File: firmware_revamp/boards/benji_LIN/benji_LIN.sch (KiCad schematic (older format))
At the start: 48 parts, among them J1 CONN_02X03, U1 MCP2561-E_SN, U101 TPS560430YF, U2 ATMEGA16M1, U3 TLIN1021DRQ1, Y1 Crystal_SMD

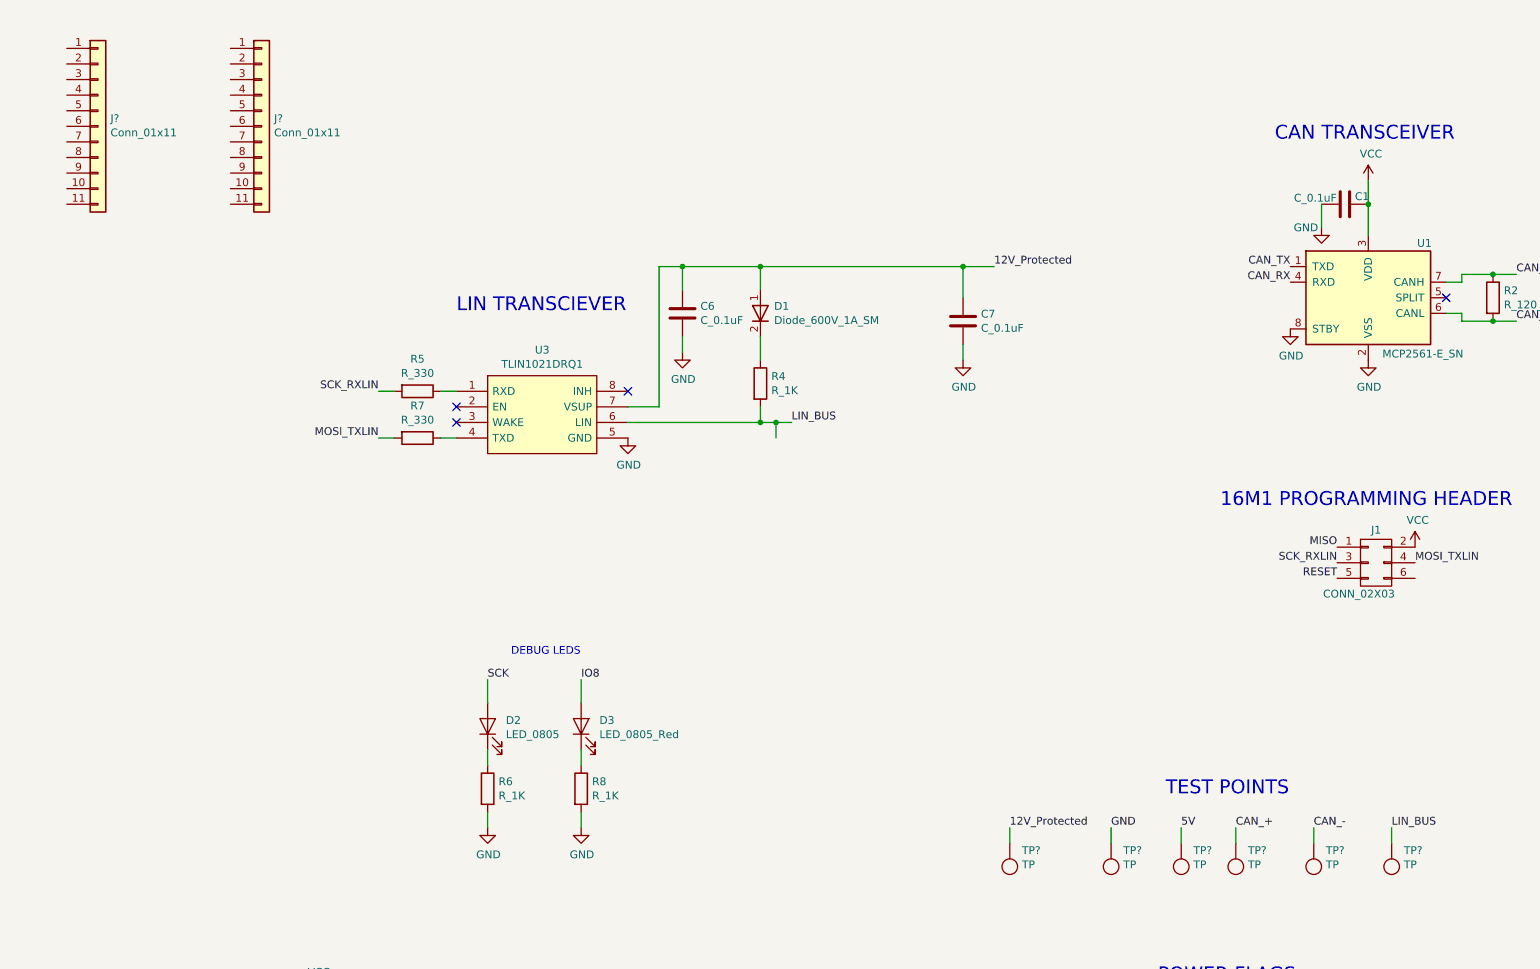
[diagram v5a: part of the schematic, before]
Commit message: Fixed name and title
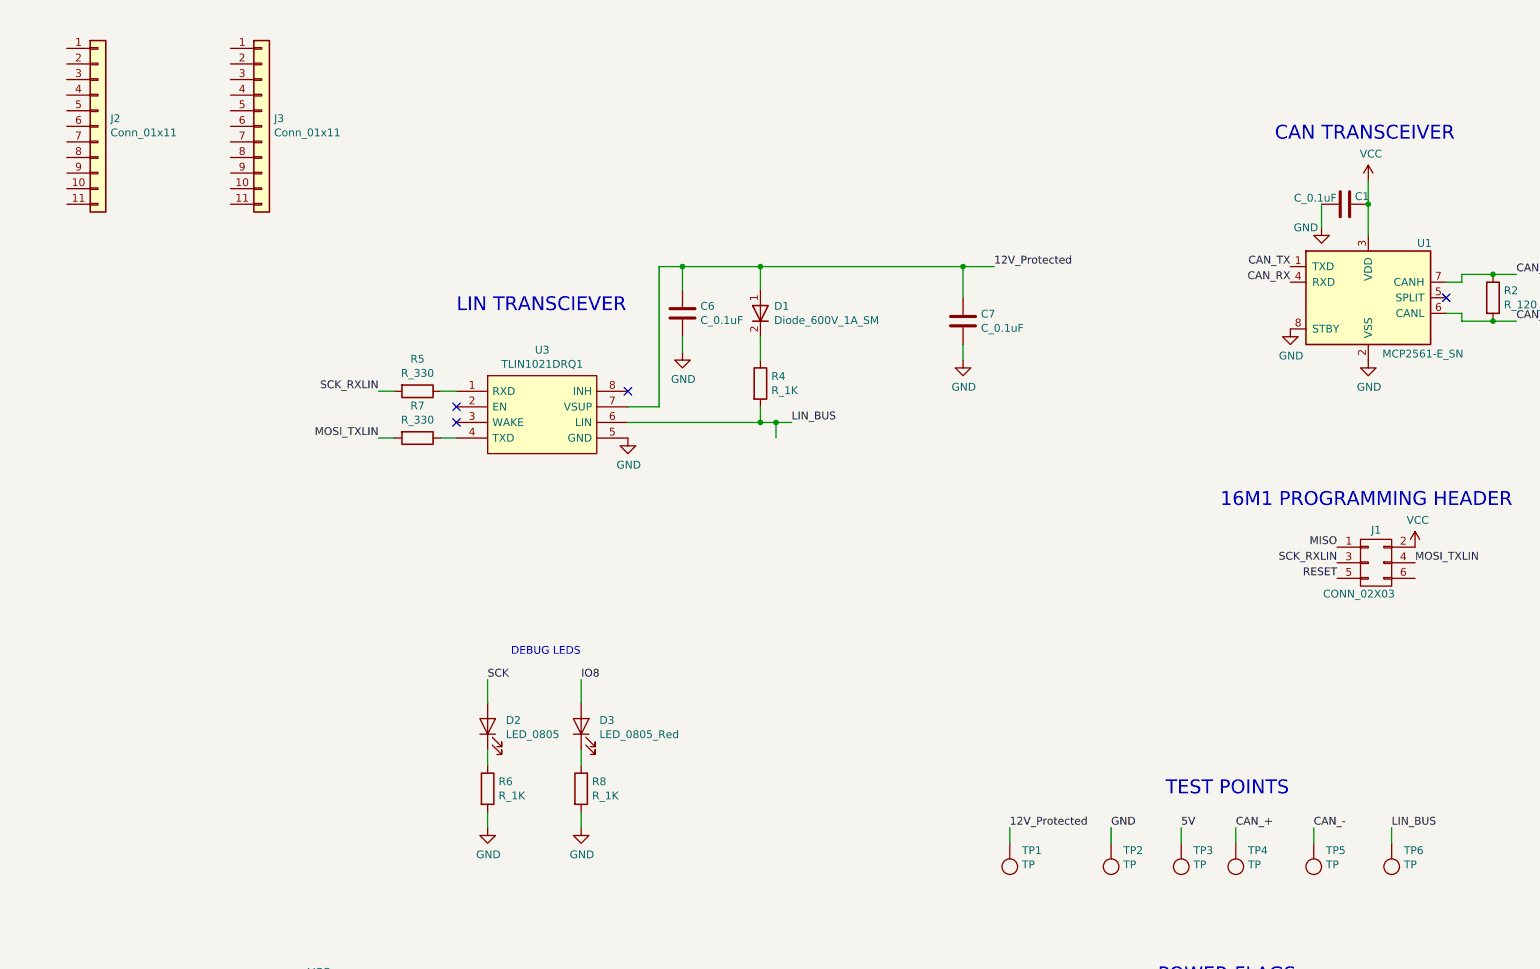
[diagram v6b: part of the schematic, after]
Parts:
- gave numbers to parts that had none: 8
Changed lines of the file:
@@
 encoding utf-8
 Sheet 1 1
-Title "OEM Project Template"
+Title "OEM LIN Hackerboard"
 Date "2019-08-22"
 Rev "1"
 Comp "Olin Electric Motorsports"
-Comment1 "Wesley Soo-Hoo"
+Comment1 "Benji Pugh"
 Comment2 ""
 Comment3 ""
@@
 	7850 3700 7950 3700
 $Comp
-L formula:Conn_01x11 J?
+L formula:Conn_01x11 J2
 U 1 1 603F6805
 P 5650 1750
-F 0 "J?" H 5730 1850 50  0000 L CNN
+F 0 "J2" H 5730 1850 50  0000 L CNN
 F 1 "Conn_01x11" H 5730 1759 50  0000 L CNN
 F 2 "footprints:PinHeader_1x11_P2.54mm_Vertical" H 5550 2450 50  0001 C CNN
@@
 $EndComp
 $Comp
-L formula:Conn_01x11 J?
+L formula:Conn_01x11 J3
 U 1 1 6040C0B1
 P 6700 1750
-F 0 "J?" H 6780 1850 50  0000 L CNN
+F 0 "J3" H 6780 1850 50  0000 L CNN
 F 1 "Conn_01x11" H 6780 1759 50  0000 L CNN
 F 2 "footprints:PinHeader_1x11_P2.54mm_Vertical" H 6600 2450 50  0001 C CNN
@@
 $EndComp
 $Comp
-L formula:TP TP?
+L formula:TP TP2
 U 1 1 6043188E
 P 12150 6500
-F 0 "TP?" H 12072 6346 50  0000 R CNN
+F 0 "TP2" H 12072 6346 50  0000 R CNN
 F 1 "TP" H 12072 6437 50  0000 R CNN
 F 2 "footprints:tp_1.6mm" H 12050 6400 50  0001 C CNN
@@
 $EndComp
 $Comp
-L formula:TP TP?
+L formula:TP TP3
 U 1 1 60452016
 P 12600 6500
-F 0 "TP?" H 12522 6346 50  0000 R CNN
+F 0 "TP3" H 12522 6346 50  0000 R CNN
 F 1 "TP" H 12522 6437 50  0000 R CNN
 F 2 "footprints:tp_1.6mm" H 12500 6400 50  0001 C CNN
@@
 $EndComp
 $Comp
-L formula:TP TP?
+L formula:TP TP4
 U 1 1 60452657
 P 12950 6500
-F 0 "TP?" H 12872 6346 50  0000 R CNN
+F 0 "TP4" H 12872 6346 50  0000 R CNN
 F 1 "TP" H 12872 6437 50  0000 R CNN
 F 2 "footprints:tp_1.6mm" H 12850 6400 50  0001 C CNN
@@
 $EndComp
 $Comp
-L formula:TP TP?
+L formula:TP TP5
 U 1 1 60452C4A
 P 13450 6500
-F 0 "TP?" H 13372 6346 50  0000 R CNN
+F 0 "TP5" H 13372 6346 50  0000 R CNN
 F 1 "TP" H 13372 6437 50  0000 R CNN
 F 2 "footprints:tp_1.6mm" H 13350 6400 50  0001 C CNN
@@
 $EndComp
 $Comp
-L formula:TP TP?
+L formula:TP TP6
 U 1 1 604534CE
 P 13950 6500
-F 0 "TP?" H 13872 6346 50  0000 R CNN
+F 0 "TP6" H 13872 6346 50  0000 R CNN
 F 1 "TP" H 13872 6437 50  0000 R CNN
 F 2 "footprints:tp_1.6mm" H 13850 6400 50  0001 C CNN
@@
 	11500 6200 11500 6300
 $Comp
-L formula:TP TP?
+L formula:TP TP1
 U 1 1 6042FA03
 P 11500 6500
-F 0 "TP?" H 11422 6346 50  0000 R CNN
+F 0 "TP1" H 11422 6346 50  0000 R CNN
 F 1 "TP" H 11422 6437 50  0000 R CNN
 F 2 "footprints:tp_1.6mm" H 11400 6400 50  0001 C CNN

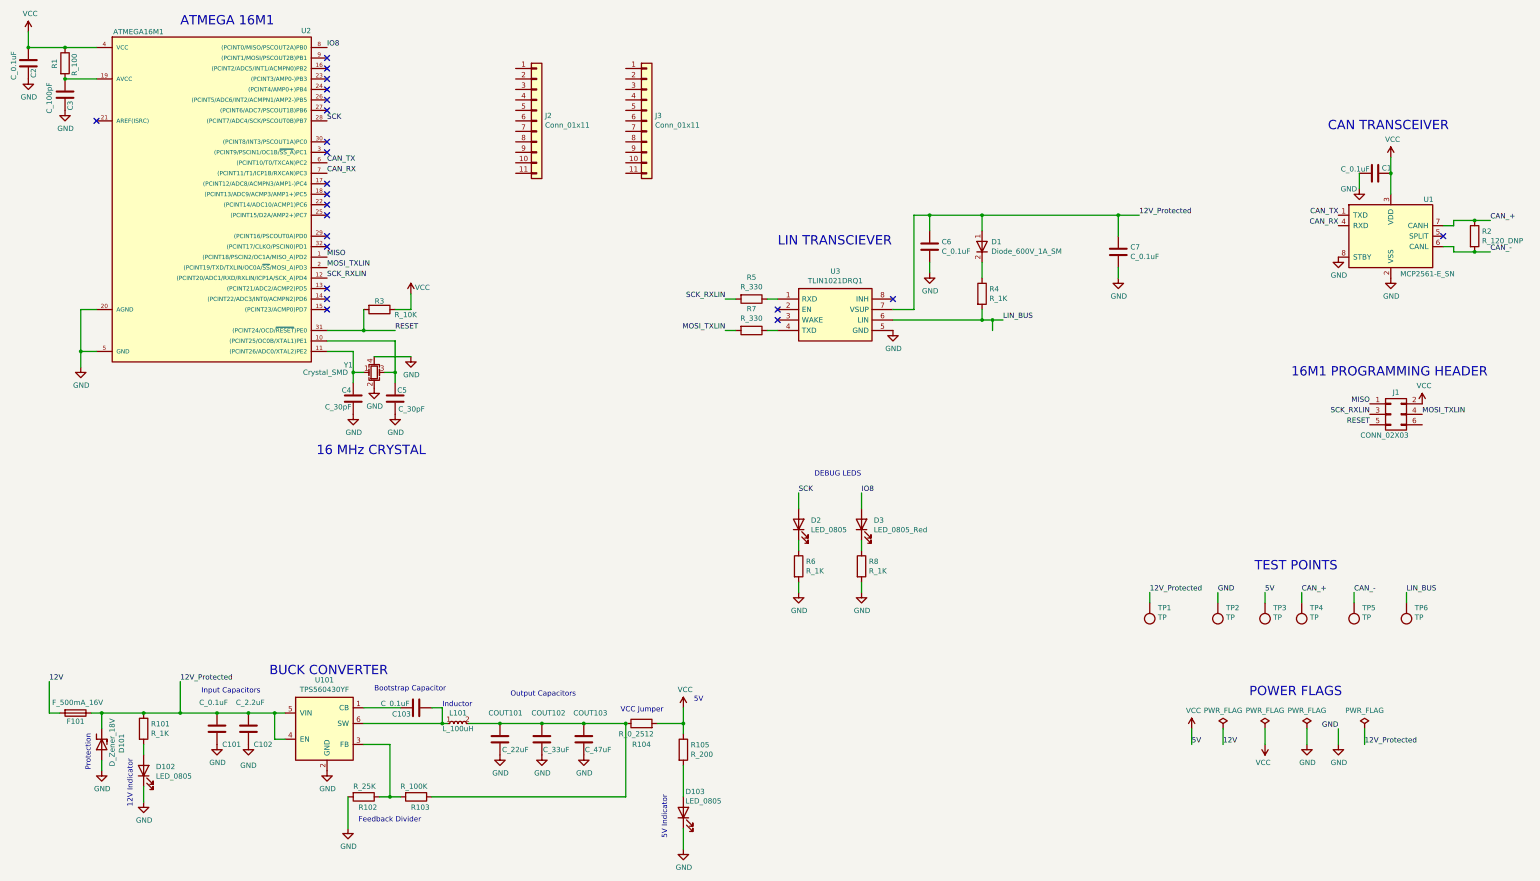
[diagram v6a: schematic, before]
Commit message: Removed Buck, Added LIN switch, changed net labels
Following the design review, the buck converter was removed, a swtich for toggling the LIN transciever was added, and net labels were adjusted. Additionally a VIN connector was added for powering the lin transciever
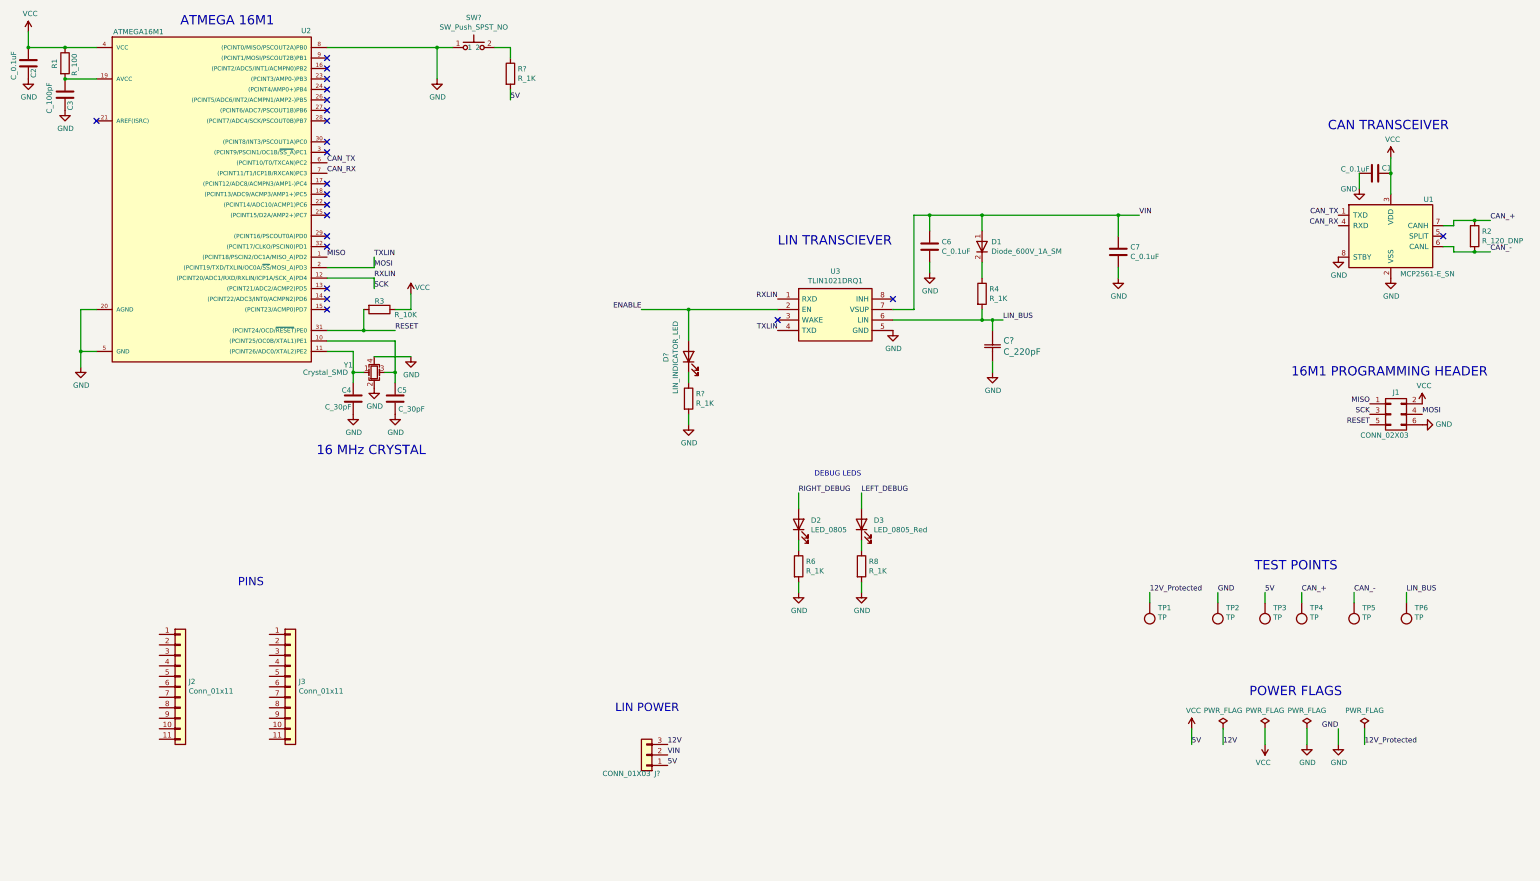
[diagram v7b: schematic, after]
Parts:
- removed C101, C103: C_0.1uF, footprints:C_0805_OEM, symbol template-rescue:C_0.1uF-formula
- removed C102: C_2.2uF, footprints:C_0603_1608Metric, symbol template-rescue:C_2.2uF-formula
- removed COUT101: C_22uF, footprints:C_1206_OEM, symbol template-rescue:C_22uF-formula
- removed COUT102: C_33uF, footprints:C_1812_OEM, symbol template-rescue:C_33uF-formula
- removed COUT103: C_47uF, footprints:C_0805_OEM, symbol template-rescue:C_47uF-formula
- removed D101: D_Zener_18V, footprints:DO-214AA, symbol template-rescue:D_Zener_18V-formula
- removed D102, D103: LED_0805, footprints:LED_0805_OEM, symbol template-rescue:LED_0805-formula
- removed F101: F_500mA_16V, footprints:Fuse_1210, symbol template-rescue:F_500mA_16V-formula
- removed L101: L_100uH, formula:L_100uH, symbol template-rescue:L_100uH-formula
- removed R101: R_1K, footprints:R_0805_OEM, symbol formula:R_1K
- removed R102: R_25K, footprints:R_0805_OEM, symbol template-rescue:R_25K-formula
- removed R103: R_100K, footprints:R_0805_OEM, symbol template-rescue:R_100K-formula
- removed R104: R_0_2512, footprints:R_2512_OEM, symbol template-rescue:R_0_2512-formula
- removed R105: R_200, footprints:R_0805_OEM, symbol template-rescue:R_200-formula
- removed R5, R7: R_330, footprints:R_0805_OEM, symbol formula:R_330
- removed U101: TPS560430YF, Package_TO_SOT_SMD:SOT-23-6_Handsoldering, symbol template-rescue:TPS560430YF-formula
- added C?: C_220pF, footprints:C_0603_1608Metric, symbol formula:C_220pF
- added D?: LIN_INDICATOR_LED, footprints:LED_0805_OEM, symbol formula:LED_0805_Amber
- added J?: CONN_01X03, Pin_Headers:Pin_Header_Straight_1x03_Pitch2.54mm, symbol formula:CONN_01X03
- added R? (x2): R_1K, footprints:R_0805_OEM, symbol formula:R_1K
- added SW?: SW_Push_SPST_NO, footprints:SW_B3U-1000P_4.2x1.7mm, symbol formula:SW_Push_SPST_NO
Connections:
- net MOSI_TXLIN is gone; now on net MOSI: J1.4 (P4), U2.2 ((PCINT19/TXD/TXLIN/OC0A/~SS~/MOSI_A)PD3)
- net SCK_RXLIN is gone; now on net RXLIN: J1.3 (P3), U2.12 ((PCINT20/ADC1/RXD/RXLIN/ICP1A/SCK_A)PD4)
- net 12V: now also J?.3 (P3)
- net 12V_Protected: no longer C6.1, C7.1, D1.1, U3.7 (VSUP)
- net GND: now also J1.6 (P6), U2.8 ((PCINT0/MISO/PSCOUT2A)PB0), C?.2, R?.2, SW?.1
- net LIN_BUS: now also C?.1
- net VCC: now also J?.1 (P1), R?.2
- net RXLIN: now reaches U3.1 (RXD)
- net ENABLE: now reaches U3.2 (EN)
- net ENABLE: now also D?.2 (A)
- net MOSI: now reaches U3.4 (TXD)
- net IO8 renamed LEFT_DEBUG
- net LEFT_DEBUG: no longer U2.8 ((PCINT0/MISO/PSCOUT2A)PB0)
- net SCK: no longer names the net of U2.28 ((PCINT7/ADC4/SCK/PSCOUT0B)PB7)
- net SCK: no longer D2.2 (A)
- new net: R?.1, SW?.2
- new net: D?.1 (K), R?.1
- new net RIGHT_DEBUG: D2.2 (A)
- new net VIN: C6.1, C7.1, D1.1, J?.2 (P2), U3.7 (VSUP)
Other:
- note added: "LIN POWER"
- note added: "PINS"
- note removed: "12V Indicator"
- note removed: "5V"
- note removed: "5V Indicator"
- note removed: "BUCK CONVERTER\n"
- note removed: "Bootstrap Capacitor\n"
- note removed: "Feedback Divider\n"
- note removed: "Inductor\n"
- note removed: "Input Capacitors\n\n"
- note removed: "Output Capacitors\n"
- note removed: "Protection\n"
- note removed: "VCC Jumper\n"
- moved on the sheet: J2, J3
